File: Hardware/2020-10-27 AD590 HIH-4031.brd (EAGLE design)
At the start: 33 x 14 mm, 5 parts, among them U1 HIH-4031

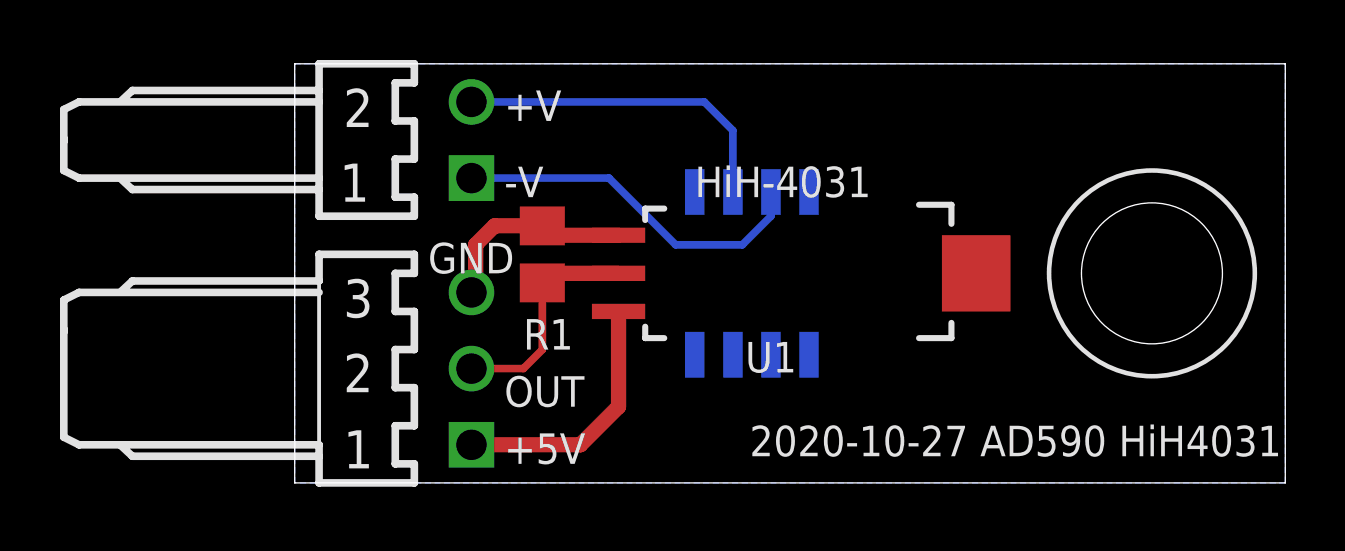
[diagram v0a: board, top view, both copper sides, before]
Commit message: Moved connectors to butt against each other
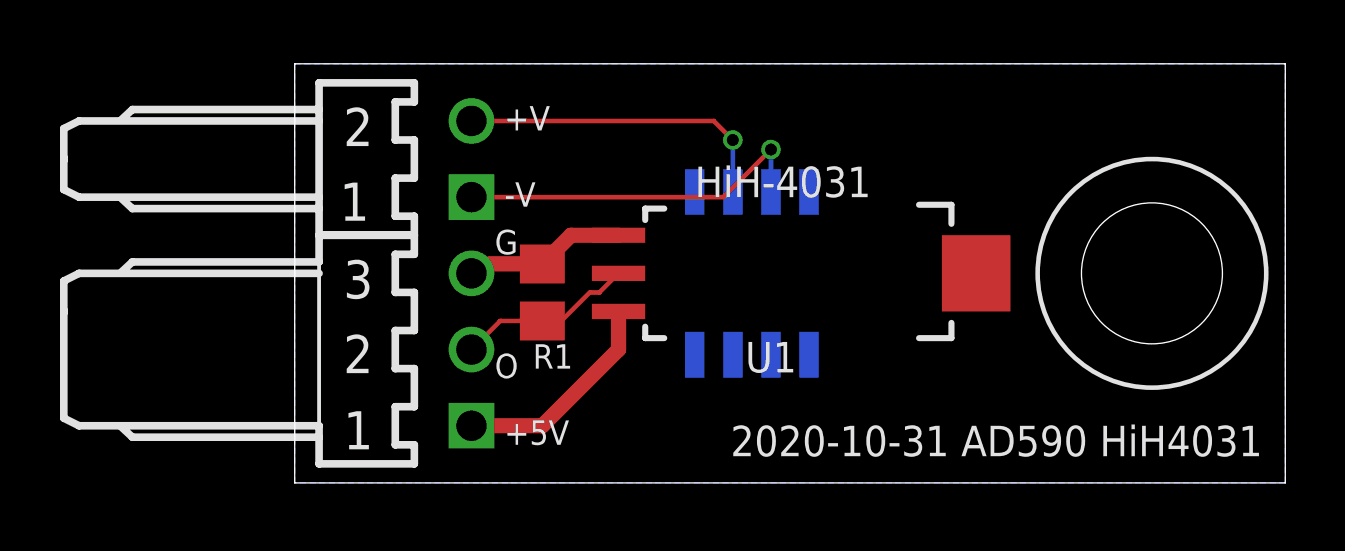
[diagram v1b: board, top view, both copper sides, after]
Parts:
- IC1: value (none) -> AD590
- moved R1 1.27 mm to (8.26, 6.35)
- moved JP2 0.64 mm to (5.89, 4.45)
- moved JP1 0.63 mm to (5.89, 10.8)
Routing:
- net OUT: track 7.52 -> 5.95 mm
- net VCC: track 8.60 -> 7.22 mm
- net GND: track 6.80 -> 5.43 mm
- net V+: track 11.2 -> 10.7 mm, vias 0 -> 1
- net V-: vias 0 -> 1
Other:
- board text added: "2020-10-31 AD590 HiH4031"
- board text added: "G"
- board text added: "O"
- board text removed: "2020-10-27 AD590 HiH4031"
